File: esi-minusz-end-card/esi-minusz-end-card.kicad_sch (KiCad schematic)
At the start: 34 parts, among them J1 J-SAMTEC-TFM-120-01-L-D-RA, J2 U.FL-R-SMT-1, J3 M55-7101242R, J5 M55-7101242R, J6 +UHF, J7 -UHF, U1 NCS2-62+

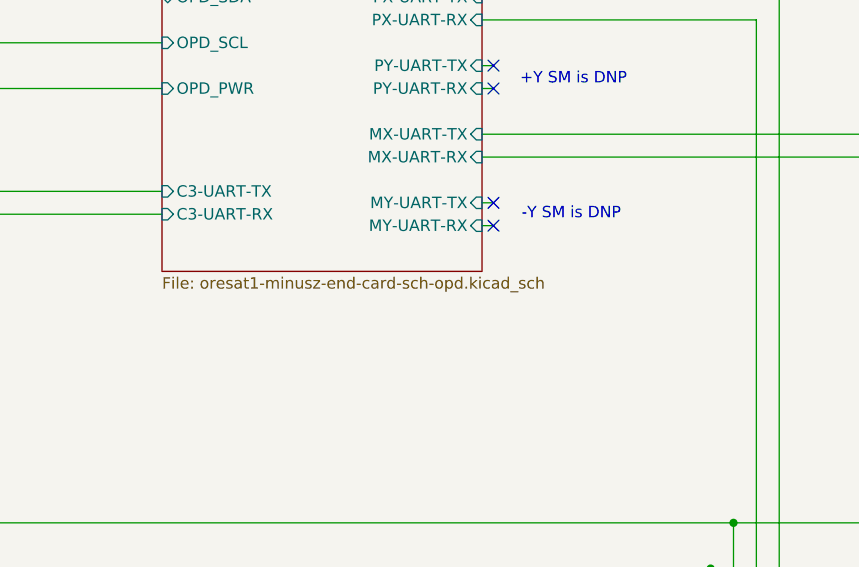
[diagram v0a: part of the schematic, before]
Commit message: renamed ESI -Z end card to combat Shae's weird naming conventions
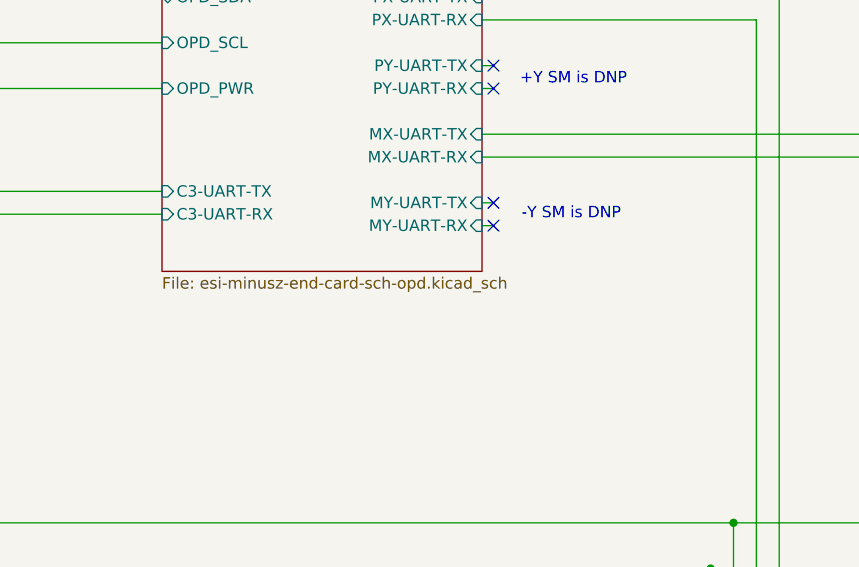
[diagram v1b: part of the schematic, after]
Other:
- sheet OPD: file oresat1-minusz-end-card-sch-opd.kicad_sch -> esi-minusz-end-card-sch-opd.kicad_sch
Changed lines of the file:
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@@
 			)
 		)
-		(property "Sheetfile" "oresat1-minusz-end-card-sch-opd.kicad_sch"
+		(property "Sheetfile" "esi-minusz-end-card-sch-opd.kicad_sch"
 			(at 137.16 83.1346 0)
 			(effects
@@
 		)
 		(instances
-			(project "ESI_minusz _end_card_v1"
+			(project "esi-minuz-end-card"
 				(path "/f7595184-4323-4ed9-b19e-5e32e3c6e76f"
 					(page "2")

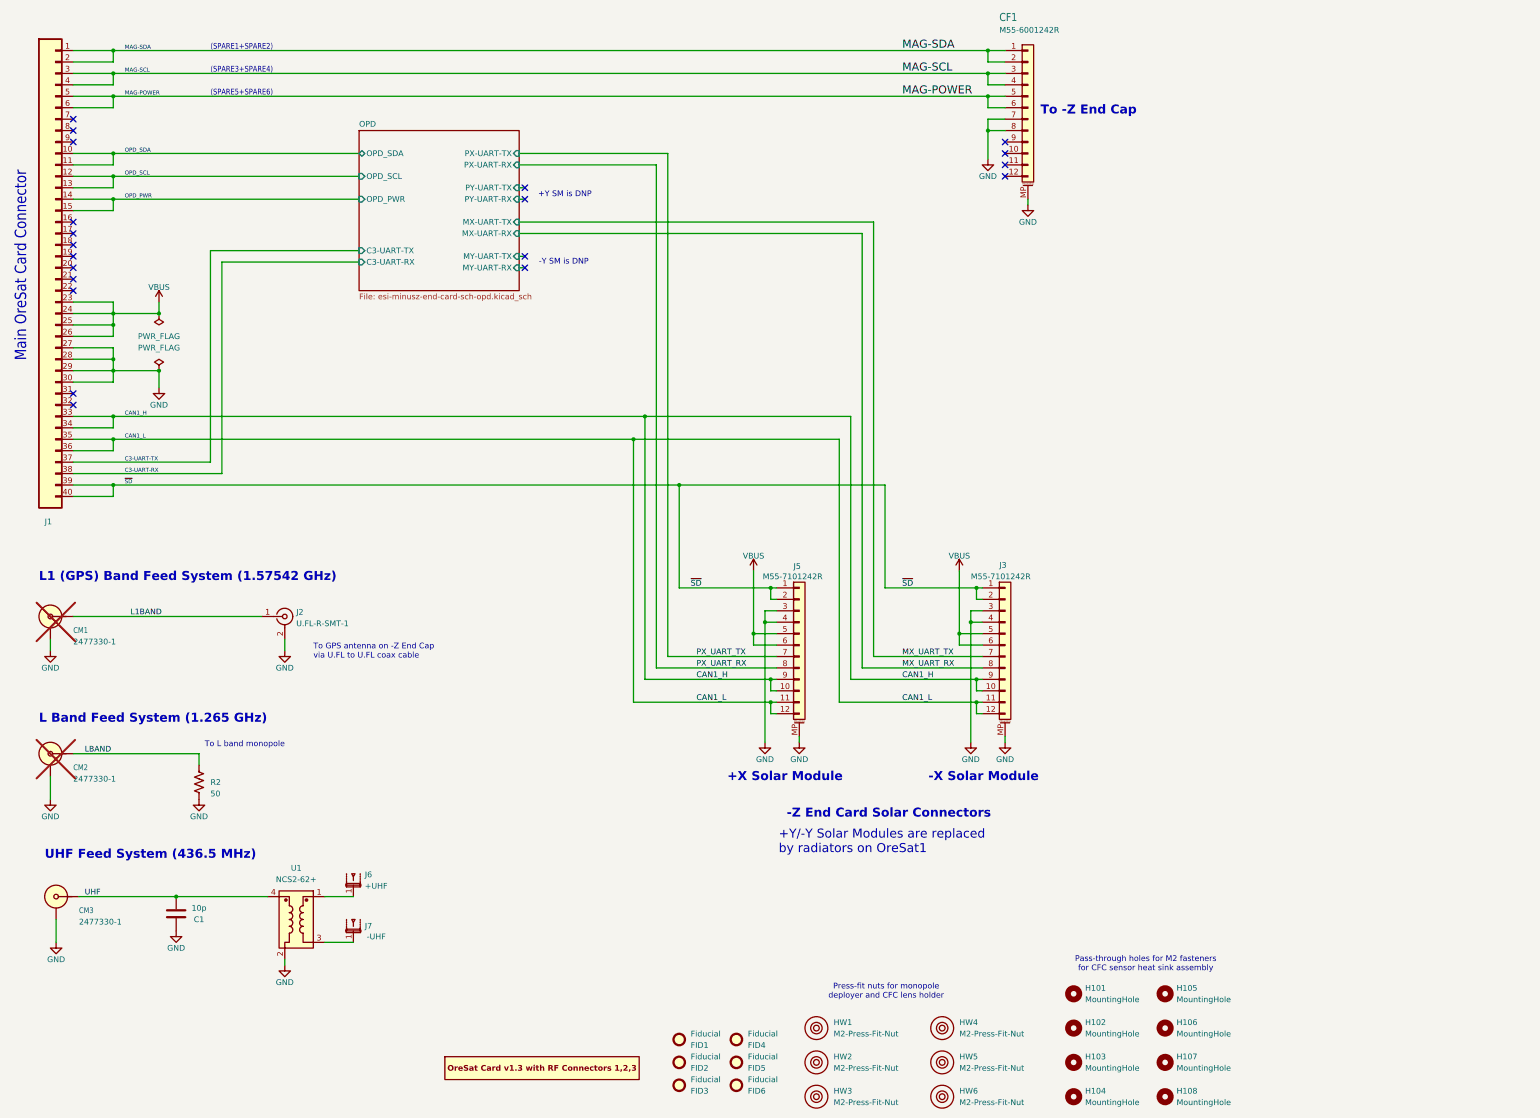
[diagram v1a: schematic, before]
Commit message: Finalized dipole changes, added -/+ Y solar mods. Believe this is finished
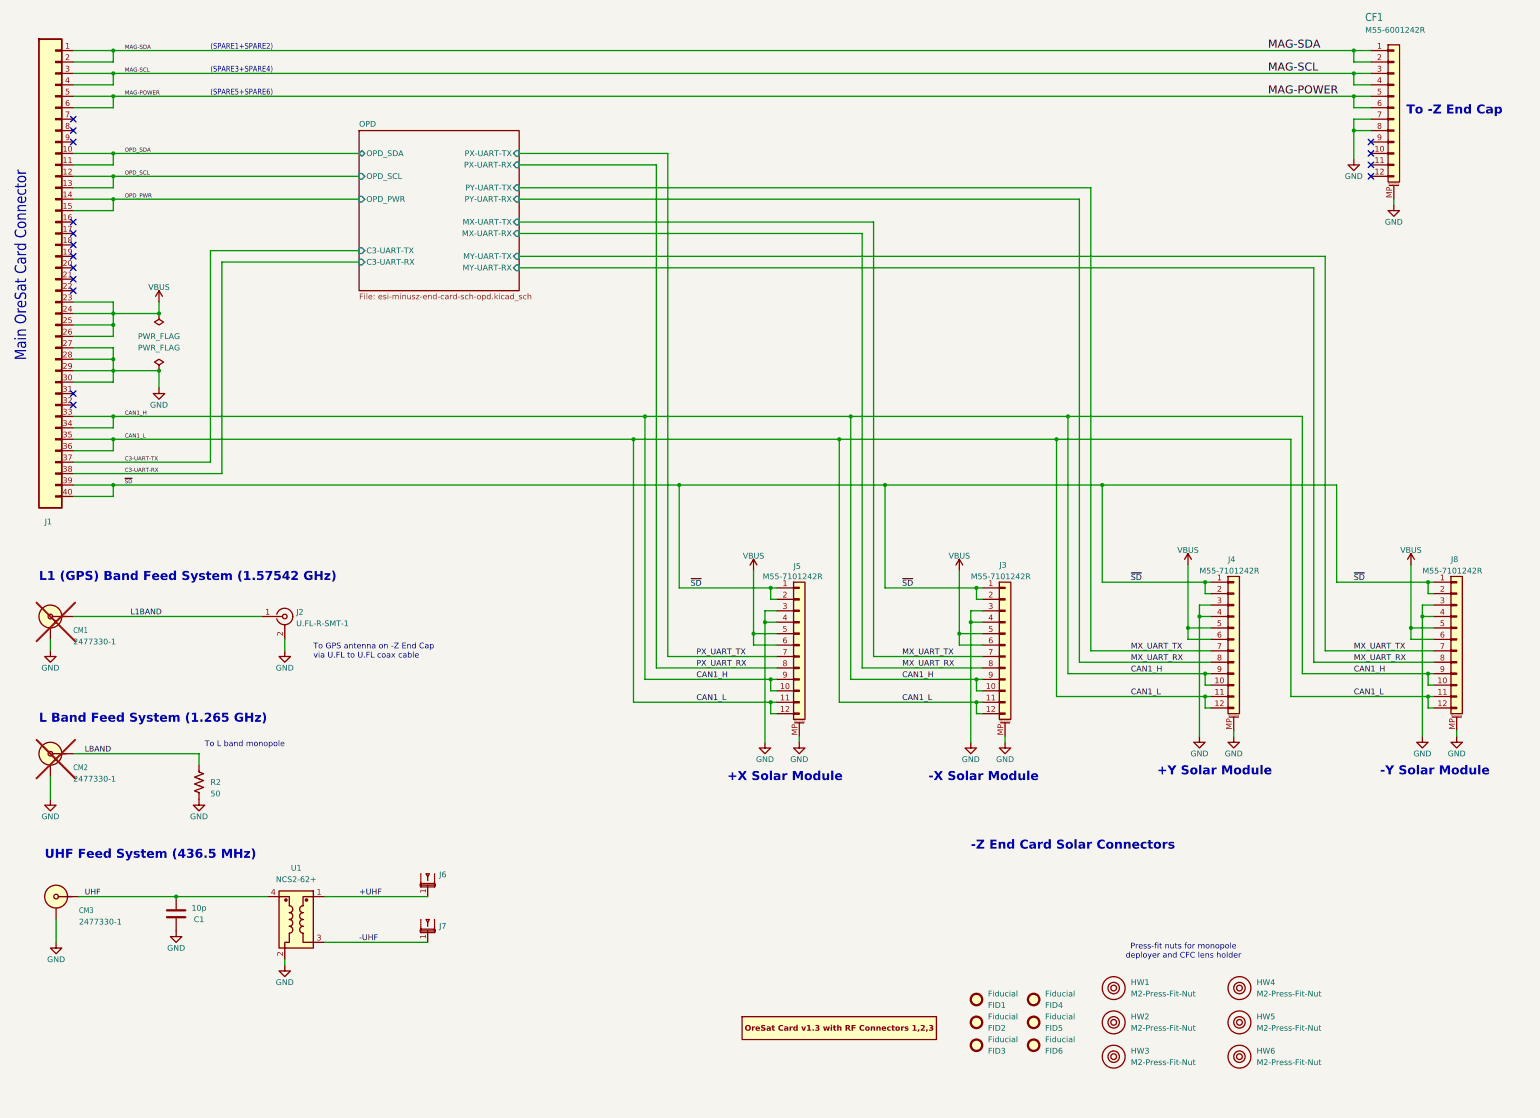
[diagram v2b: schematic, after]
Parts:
- removed H101, H102, H103, H104, H105, H106, H107, H108: MountingHole, MountingHole:MountingHole_5mm, symbol Mechanical:MountingHole
- added J4, J8: M55-7101242R, oresat-connectors:J-Harwin-M55-7101242R, symbol Connector_Generic_MountingPin:Conn_01x12_MountingPin
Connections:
- net CAN1_H: now also J4.10 (Pin_10), J4.9 (Pin_9), J8.10 (Pin_10), J8.9 (Pin_9)
- net CAN1_L: now also J4.11 (Pin_11), J4.12 (Pin_12), J8.11 (Pin_11), J8.12 (Pin_12)
- net GND: now also J4.3 (Pin_3), J4.4 (Pin_4), J4.MP (MountPin), J8.3 (Pin_3), J8.4 (Pin_4), J8.MP (MountPin)
- net MX_UART_RX: now also J4.8 (Pin_8), J8.8 (Pin_8)
- net MX_UART_TX: now also J4.7 (Pin_7), J8.7 (Pin_7)
- net VBUS: now also J4.5 (Pin_5), J4.6 (Pin_6), J8.5 (Pin_5), J8.6 (Pin_6)
- net ~{SD}: now also J4.1 (Pin_1), J4.2 (Pin_2), J8.1 (Pin_1), J8.2 (Pin_2)
- net -UHF: now reaches J7.1, U1.3
- net +UHF: now reaches J6.1, U1.1
- no-connect marks 20 -> 16
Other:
- note added: "+Y Solar Module"
- note added: "-Y Solar Module"
- note removed: "+Y SM is DNP"
- note removed: "+Y/-Y Solar Modules are replaced by radiators on OreSat1"
- note removed: "-Y SM is DNP"
- note removed: "Pass-through holes for M2 fasteners for CFC sensor heat sink assembly"
- moved on the sheet: CF1, FID1, FID2, FID3, FID4, FID5, FID6, HW1, HW2, HW3, HW4, HW5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

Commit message: Fixed OPD connection in schematics and updated tracing and out of date footprints. Ready for final review from andrew
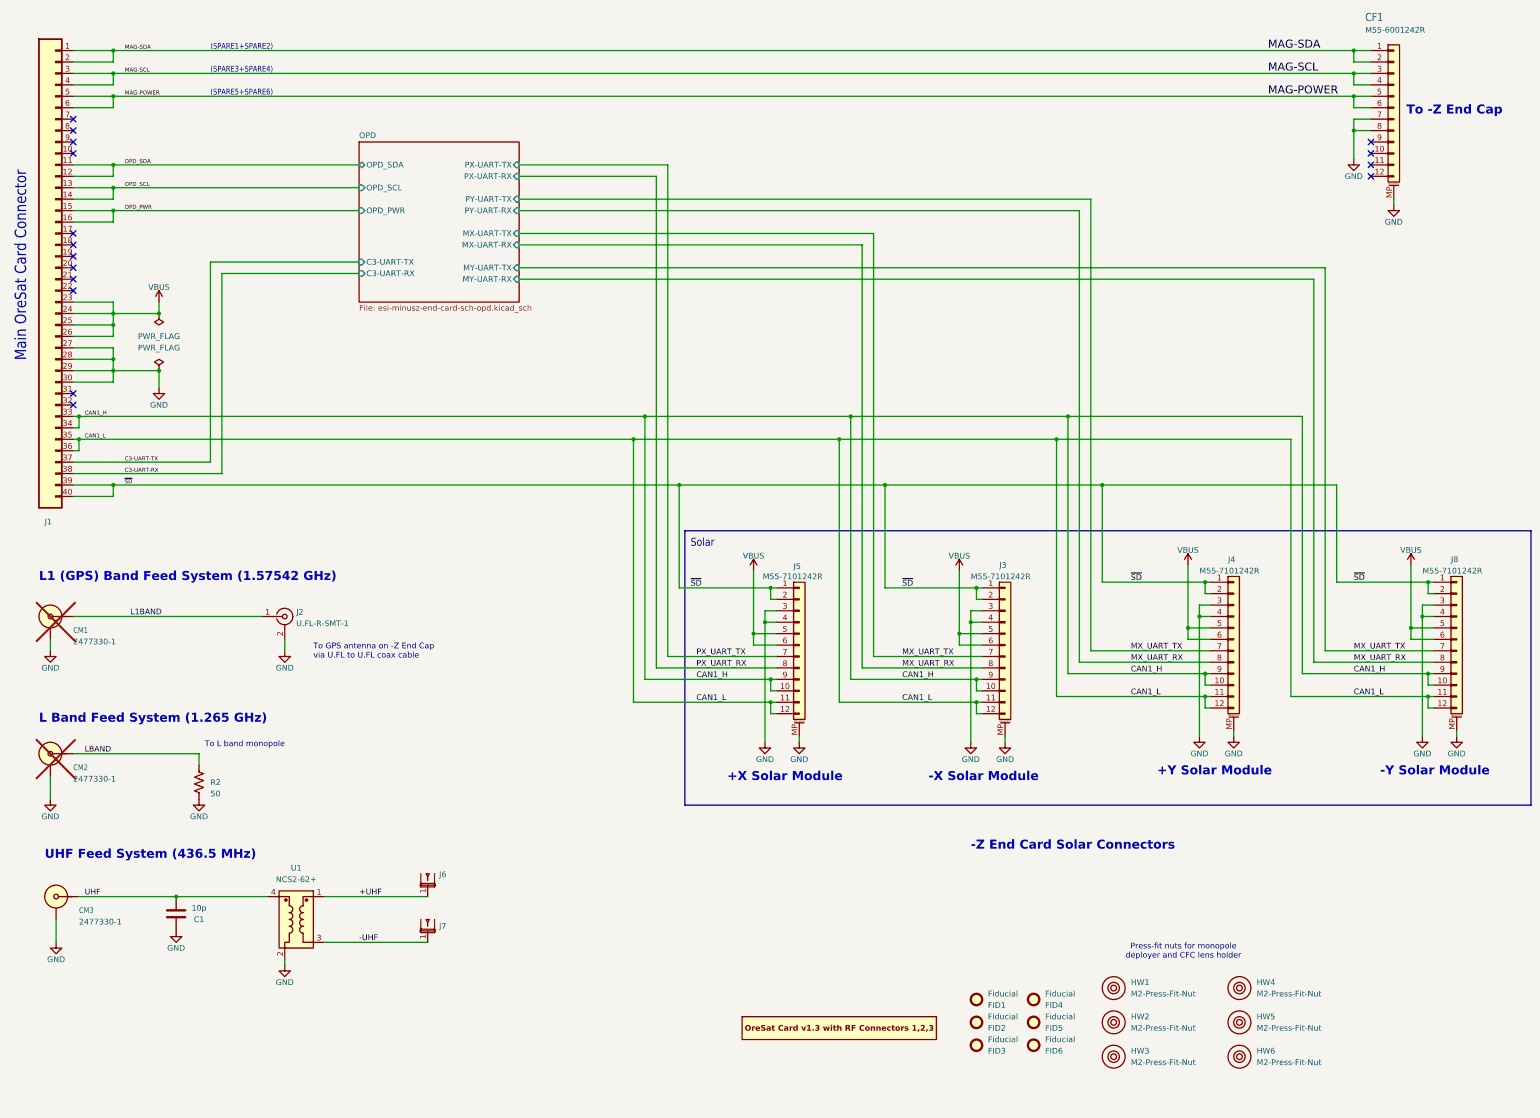
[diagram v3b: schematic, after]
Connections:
- net OPD_PWR: now also J1.16; no longer J1.14
- net OPD_SCL: now also J1.14; no longer J1.12
- net OPD_SDA: now also J1.12; no longer J1.10
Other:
- note added: "Solar"

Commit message: ESI v1.0 -Z End Card for fab
Added makefile and readme, fixed BOM error, moved to better RF zone rules
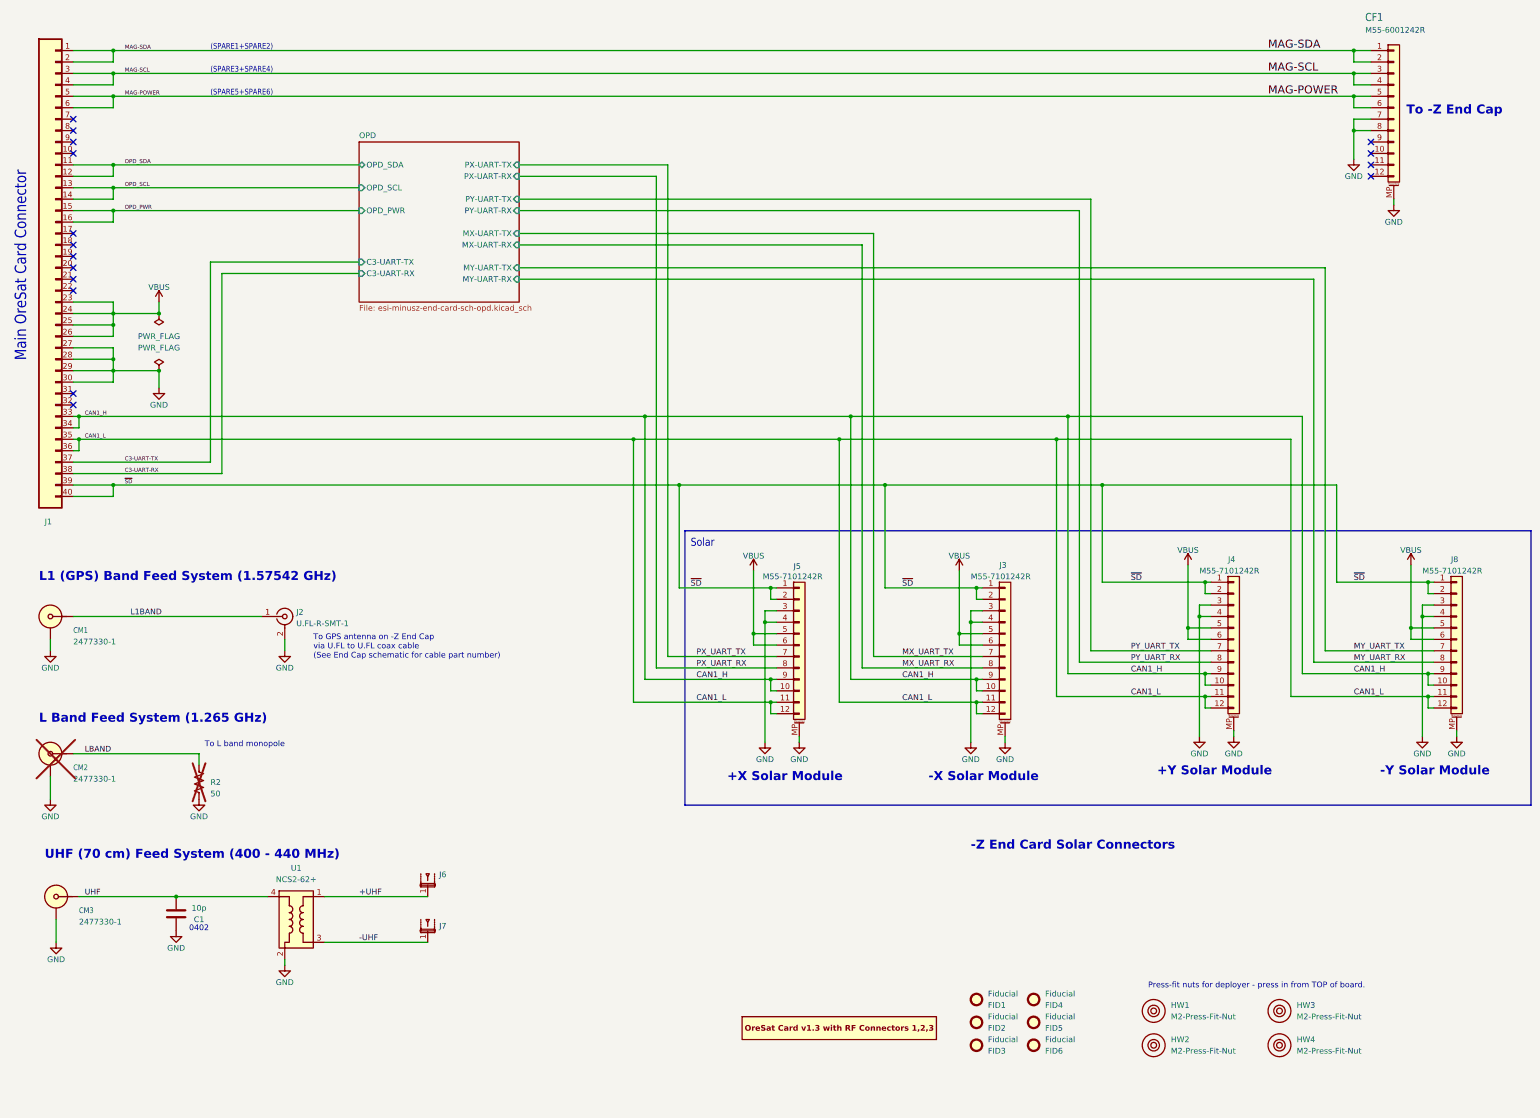
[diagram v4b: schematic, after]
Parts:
- removed HW5, HW6: M2-Press-Fit-Nut, oresat-misc:M2-Press-Fit-Nut, symbol oresat-misc:M2-Press-Fit-Nut
- C1: DIS (none) -> DigiKey; DPN (none) -> 399-16008-1-ND; MFR (none) -> KEMET; MPN (none) -> C0402C100J5GACAUTO
- CM1: now fitted
- R2: now not fitted
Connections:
- net MX_UART_RX: no longer J4.8 (Pin_8), J8.8 (Pin_8)
- net MX_UART_TX: no longer J4.7 (Pin_7), J8.7 (Pin_7)
- new net MY_UART_RX: J8.8 (Pin_8)
- new net MY_UART_TX: J8.7 (Pin_7)
- new net PY_UART_RX: J4.8 (Pin_8)
- new net PY_UART_TX: J4.7 (Pin_7)
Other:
- note added: "0402"
- note added: "Press-fit nuts for deployer - press in from TOP of board."
- note added: "To GPS antenna on -Z End Cap via U.FL to U.FL coax cable (See End Cap schematic for cable part number)"
- note added: "UHF (70 cm) Feed System (400 - 440 MHz)"
- note removed: "Press-fit nuts for monopole deployer and CFC lens holder"
- note removed: "To GPS antenna on -Z End Cap via U.FL to U.FL coax cable"
- note removed: "UHF Feed System (436.5 MHz)"
- title: OreSat1 -Z End Card -> ESI -Z End Card
- moved on the sheet: HW1, HW2, HW3, HW4
